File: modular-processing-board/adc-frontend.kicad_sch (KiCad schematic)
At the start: 65 parts, among them J601 Conn_Coaxial_Small, J604 Conn_Coaxial_Small, U1002 THS4521IDGK, U601 LMV321, U602 TL432DBZ, U603 THS4521IDGK

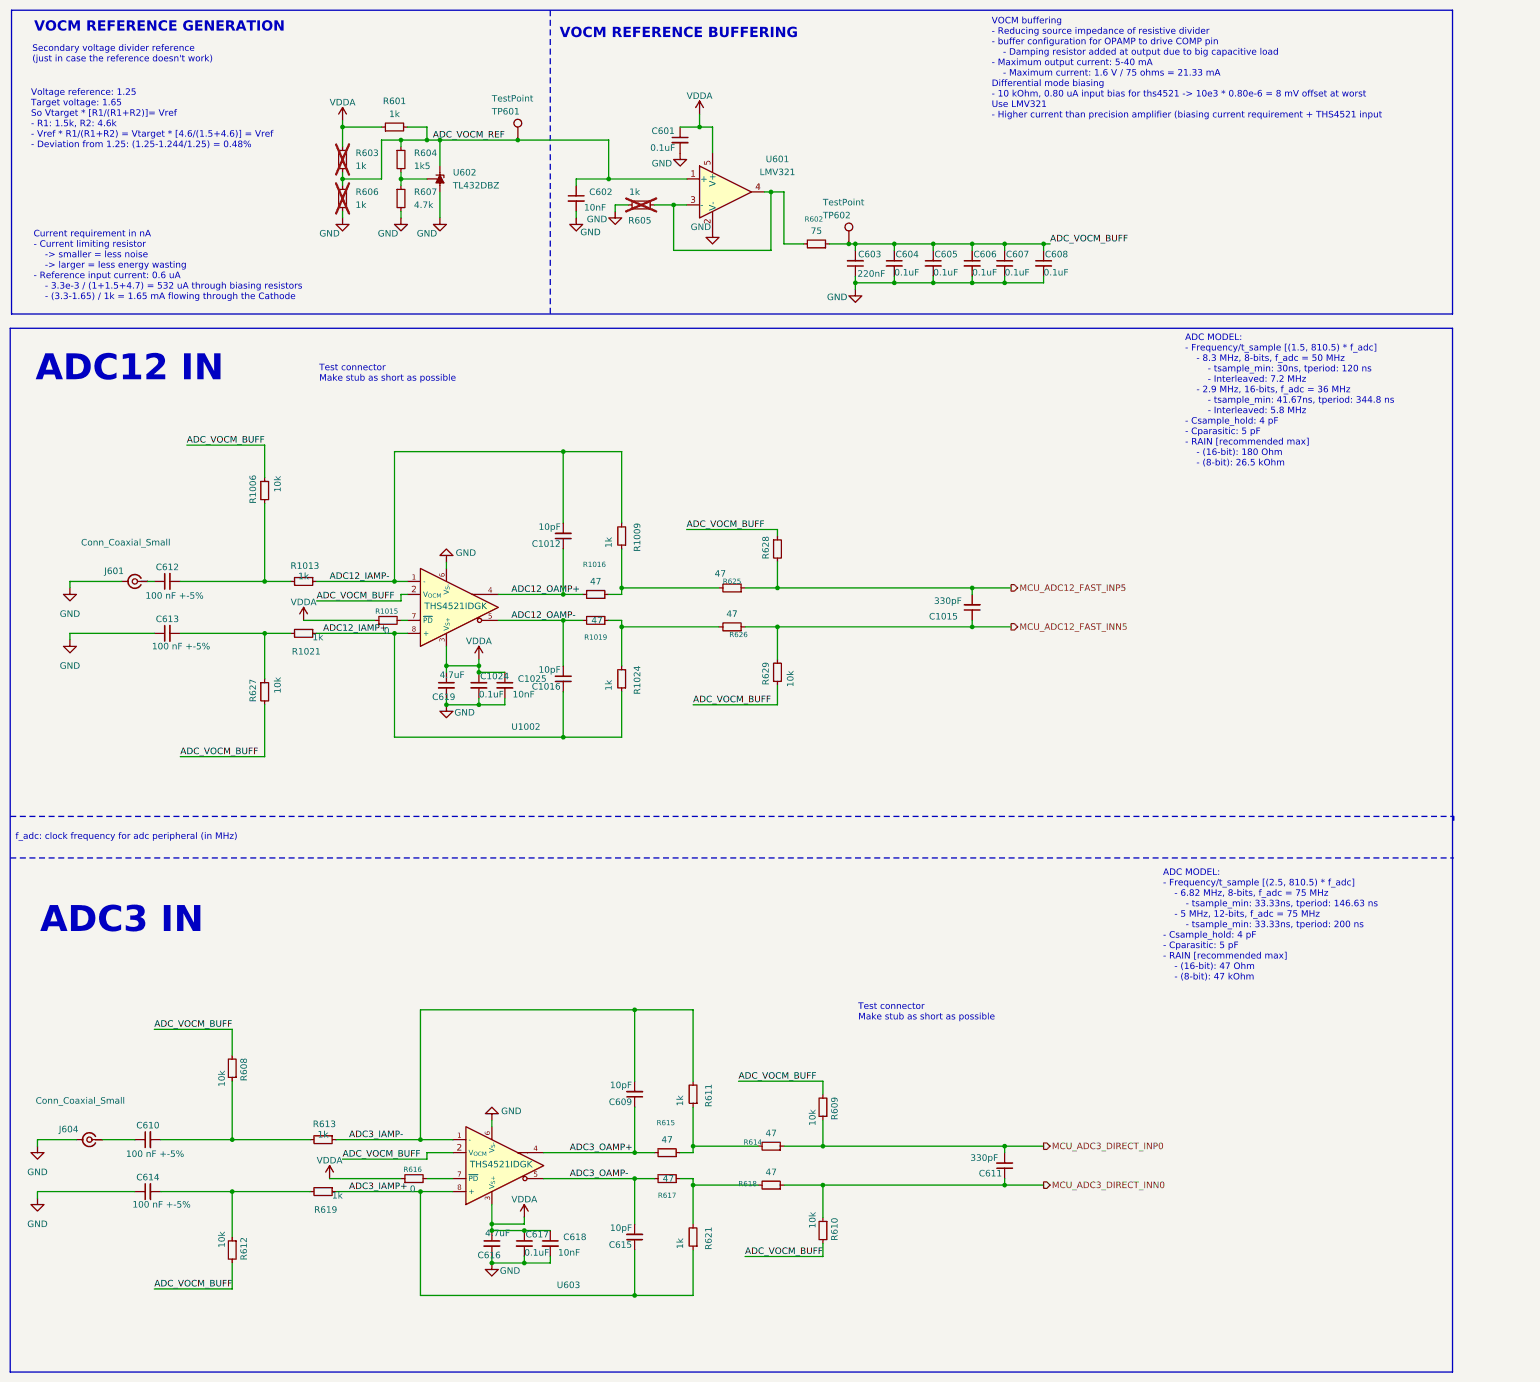
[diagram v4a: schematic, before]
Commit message: replaced sdmmc connector, added smmc trace, added u.fl. connectors
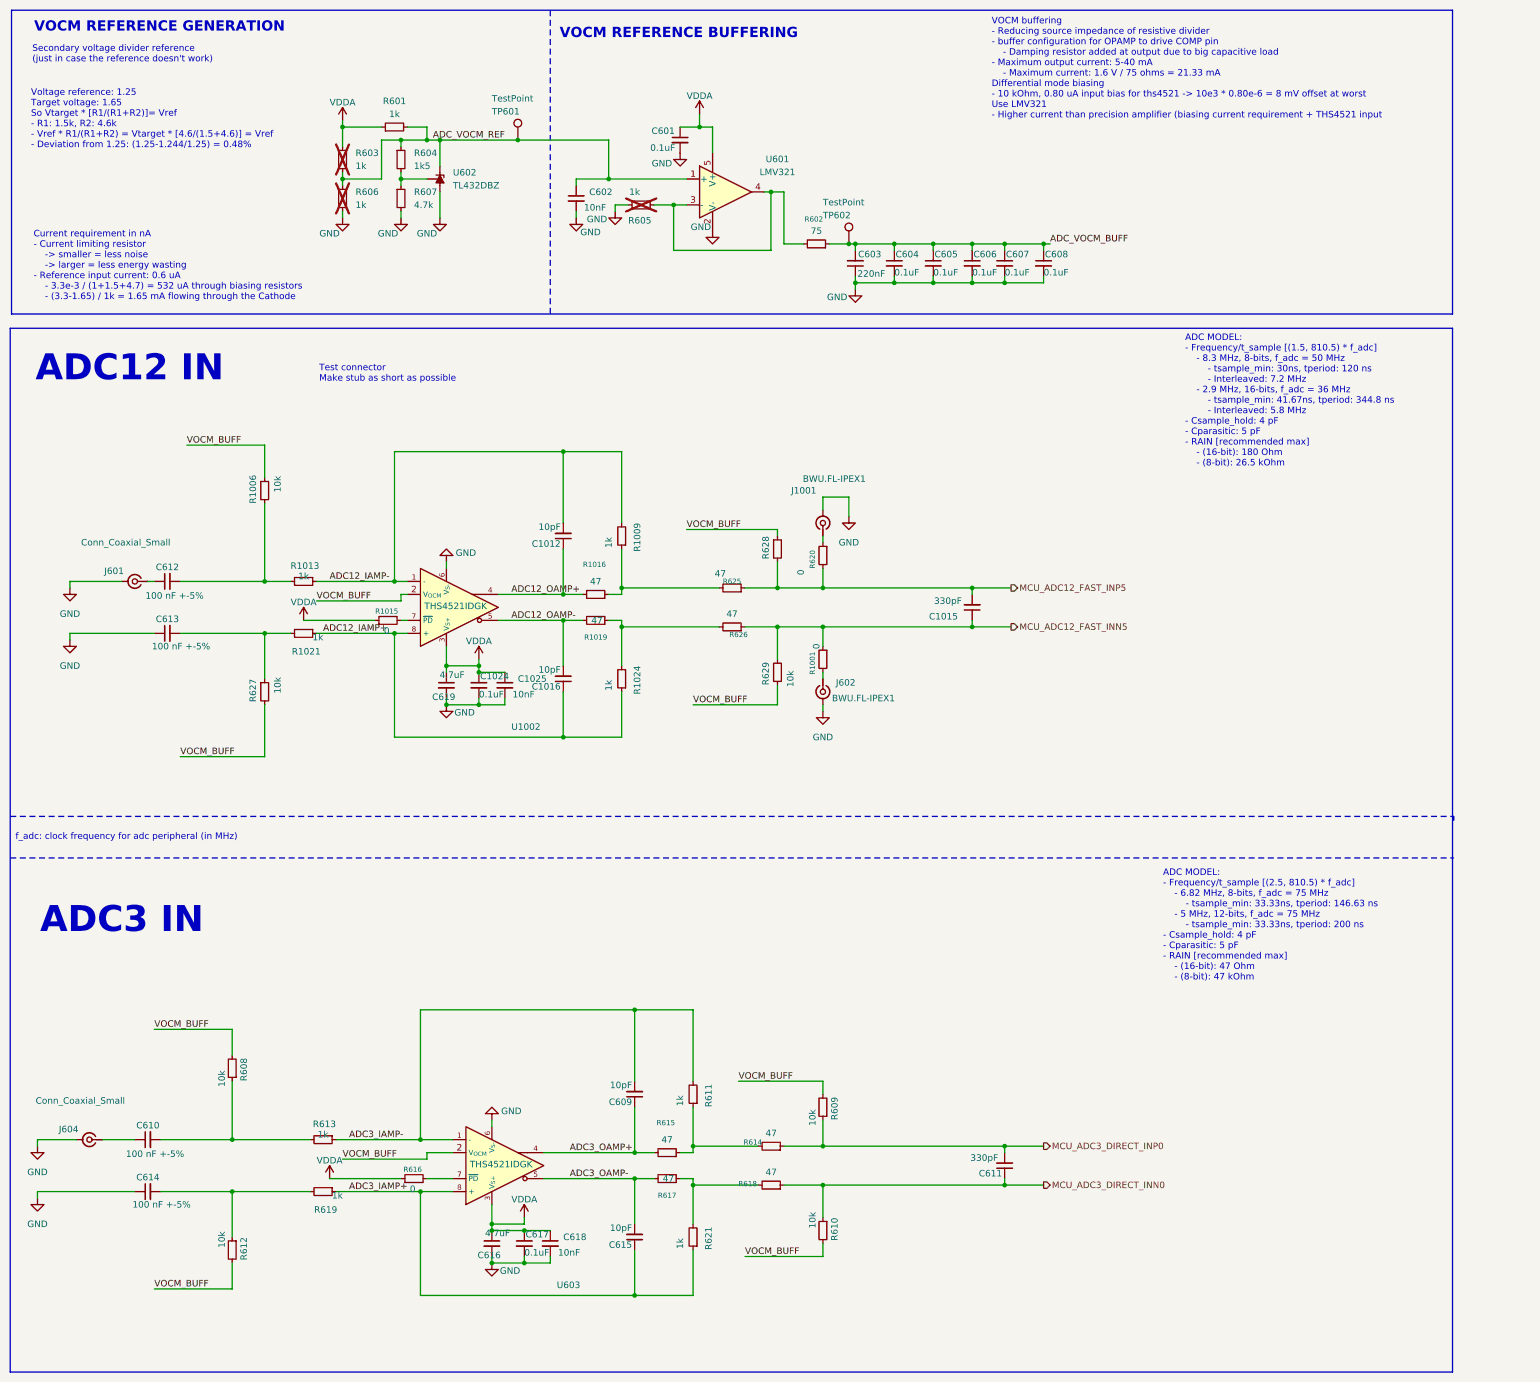
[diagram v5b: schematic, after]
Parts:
- added J1001, J602: BWU.FL-IPEX1, iw-connector:BWU.FL-IPEX1, symbol Connector:Conn_Coaxial_Small
- added R1001, R620: 0, Resistor_SMD:R_0603_1608Metric_Pad0.98x0.95mm_HandSolder, symbol Device:R_Small
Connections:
- net ADC_VOCM_BUFF: no longer R1006.1, R608.2, R609.2, R610.2, R612.2, R627.2, R628.1, R629.1, U1002.2 (V_{OCM}), U603.2 (V_{OCM})
- net GND: now also J1001.2 (Ext), J602.2 (Ext)
- net MCU_ADC12_FAST_INN5: now also R1001.1
- net MCU_ADC12_FAST_INP5: now also R620.2
- new net: J602.1 (In), R1001.2
- new net: J1001.1 (In), R620.1
- new net VOCM_BUFF: R1006.1, R608.2, R609.2, R610.2, R612.2, R627.2, R628.1, R629.1, U1002.2 (V_{OCM}), U603.2 (V_{OCM})

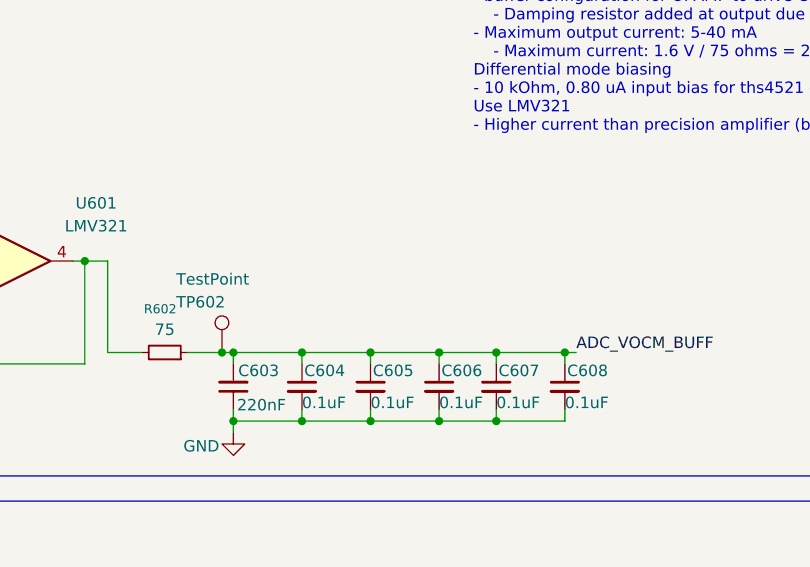
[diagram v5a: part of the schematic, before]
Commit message: reconnected vref
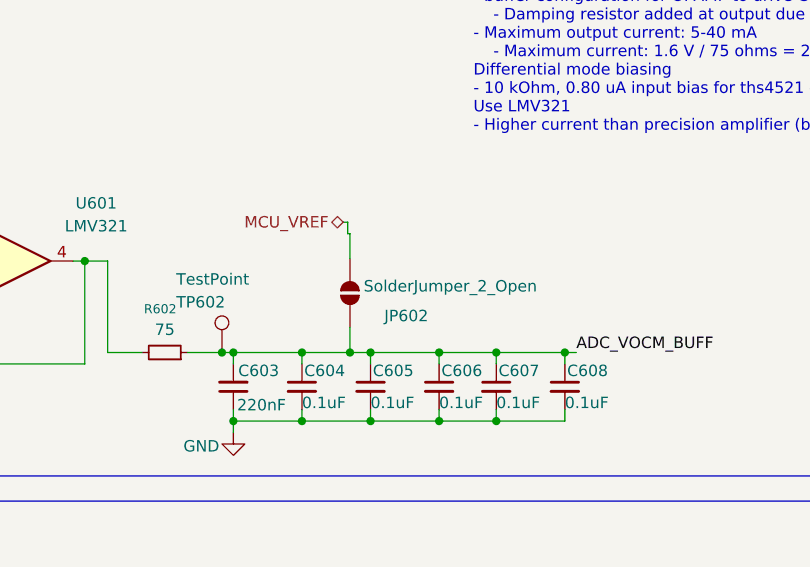
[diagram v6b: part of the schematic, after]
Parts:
- added JP602: SolderJumper_2_Open, Jumper:SolderJumper-2_P1.3mm_Open_Pad1.0x1.5mm, symbol Jumper:SolderJumper_2_Open
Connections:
- net ADC_VOCM_BUFF: now also JP602.1 (A)
- new net MCU_VREF: JP602.2 (B)
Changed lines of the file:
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@@
 	)
 	(junction
+		(at 194.564 59.69)
+		(diameter 0)
+		(color 0 0 0 0)
+	)
+	(junction
 		(at 189.23 67.31)
 		(diameter 0)
@@
 	(wire
 		(pts
+			(xy 189.23 59.69) (xy 194.564 59.69)
+		)
+		(stroke
+			(width 0)
+			(type default)
+		)
+	)
+	(wire
+		(pts
 			(xy 204.47 67.31) (xy 210.82 67.31)
 		)
@@
 	(wire
 		(pts
+			(xy 193.802 45.212) (xy 194.31 45.212)
+		)
+		(stroke
+			(width 0)
+			(type default)
+		)
+	)
+	(wire
+		(pts
 			(xy 100.33 54.61) (xy 100.33 49.53)
 		)
@@
 	(wire
 		(pts
+			(xy 194.31 45.212) (xy 194.31 46.482)
+		)
+		(stroke
+			(width 0)
+			(type default)
+		)
+	)
+	(wire
+		(pts
 			(xy 66.04 110.49) (xy 66.04 125.73)
 		)
@@
 	(wire
 		(pts
+			(xy 194.564 46.482) (xy 194.31 46.482)
+		)
+		(stroke
+			(width 0)
+			(type default)
+		)
+	)
+	(wire
+		(pts
 			(xy 135.89 147.32) (xy 135.89 156.21)
 		)
@@
 	(wire
 		(pts
+			(xy 194.564 56.896) (xy 194.564 59.69)
+		)
+		(stroke
+			(width 0)
+			(type default)
+		)
+	)
+	(wire
+		(pts
 			(xy 92.71 46.99) (xy 97.79 46.99)
 		)
@@
 	(wire
 		(pts
-			(xy 196.85 59.69) (xy 189.23 59.69)
+			(xy 180.34 59.69) (xy 181.61 59.69)
 		)
 		(stroke
@@
 	(wire
 		(pts
-			(xy 180.34 59.69) (xy 181.61 59.69)
+			(xy 160.02 127) (xy 166.37 127)
 		)
 		(stroke
@@
 	(wire
 		(pts
-			(xy 160.02 127) (xy 166.37 127)
+			(xy 138.43 237.49) (xy 142.24 237.49)
 		)
 		(stroke
@@
 	(wire
 		(pts
-			(xy 138.43 237.49) (xy 142.24 237.49)
+			(xy 194.564 59.69) (xy 196.85 59.69)
+		)
+		(stroke
+			(width 0)
+			(type default)
+		)
+	)
+	(wire
+		(pts
+			(xy 194.564 46.482) (xy 194.564 49.276)
 		)
 		(stroke
@@
 		)
 	)
+	(hierarchical_label "MCU_VREF"
+		(shape bidirectional)
+		(at 193.802 45.212 180)
+		(effects
+			(font
+				(size 1.27 1.27)
+			)
+			(justify right)
+		)
+	)
 	(hierarchical_label "MCU_ADC3_DIRECT_INP0"
 		(shape output)
@@
 					(unit 1)
 				)
+			)
+		)
+	)
+	(symbol
+		(lib_id "Jumper:SolderJumper_2_Open")
+		(at 194.564 53.086 90)
+		(unit 1)
+		(exclude_from_sim no)
+		(in_bom no)
+		(on_board yes)
+		(dnp no)
+		(property "Reference" "JP602"
+			(at 198.374 55.6259 90)
+			(effects
+				(font
+					(size 1.27 1.27)
+				)
+				(justify right)
+			)
+		)
+		(property "Value" "SolderJumper_2_Open"
+			(at 196.088 52.3239 90)
+			(effects
+				(font
+					(size 1.27 1.27)
+				)
+				(justify right)
+			)
+		)
+		(property "Footprint" "Jumper:SolderJumper-2_P1.3mm_Open_Pad1.0x1.5mm"
+			(at 194.564 53.086 0)
+			(effects
+				(font
+					(size 1.27 1.27)
+				)
+				(hide yes)
+			)
+		)
+		(property "Datasheet" "~"
+			(at 194.564 53.086 0)
+			(effects
+				(font
+					(size 1.27 1.27)
+				)
+				(hide yes)
+			)
+		)
+		(property "Description" "Solder Jumper, 2-pole, open"
+			(at 194.564 53.086 0)
+			(effects
+				(font
+					(size 1.27 1.27)
+				)
+				(hide yes)
+			)
+		)
+		(pin "2"
+		)
+		(pin "1"
+		)
+		(instances
+			(project "modular-processing-board"
+				(path "/73b5a92f-908b-4f97-a96c-14ee20a7f293/f6ec5a2c-a447-41c5-b01d-0cfa4d0577c8"
+					(reference "JP602")
+					(unit 1)
+				)

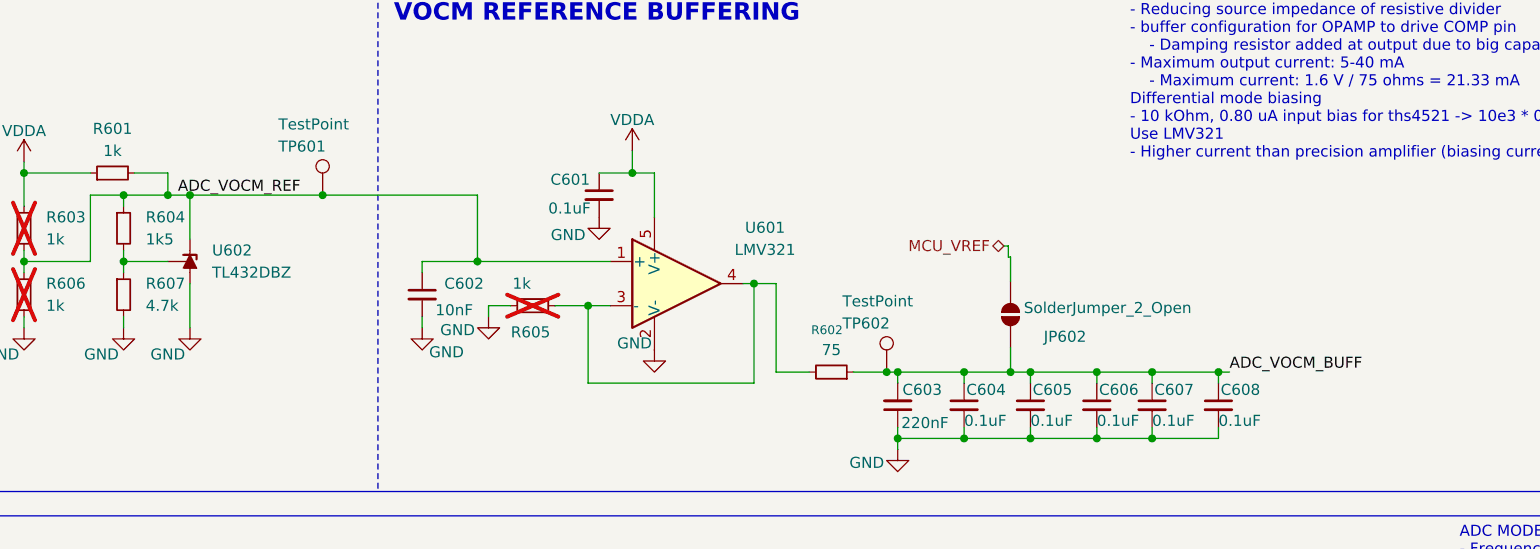
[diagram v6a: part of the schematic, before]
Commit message: layed out most components (next) cadd vias for impedance reduction for high-speed signals, check impedance of signals
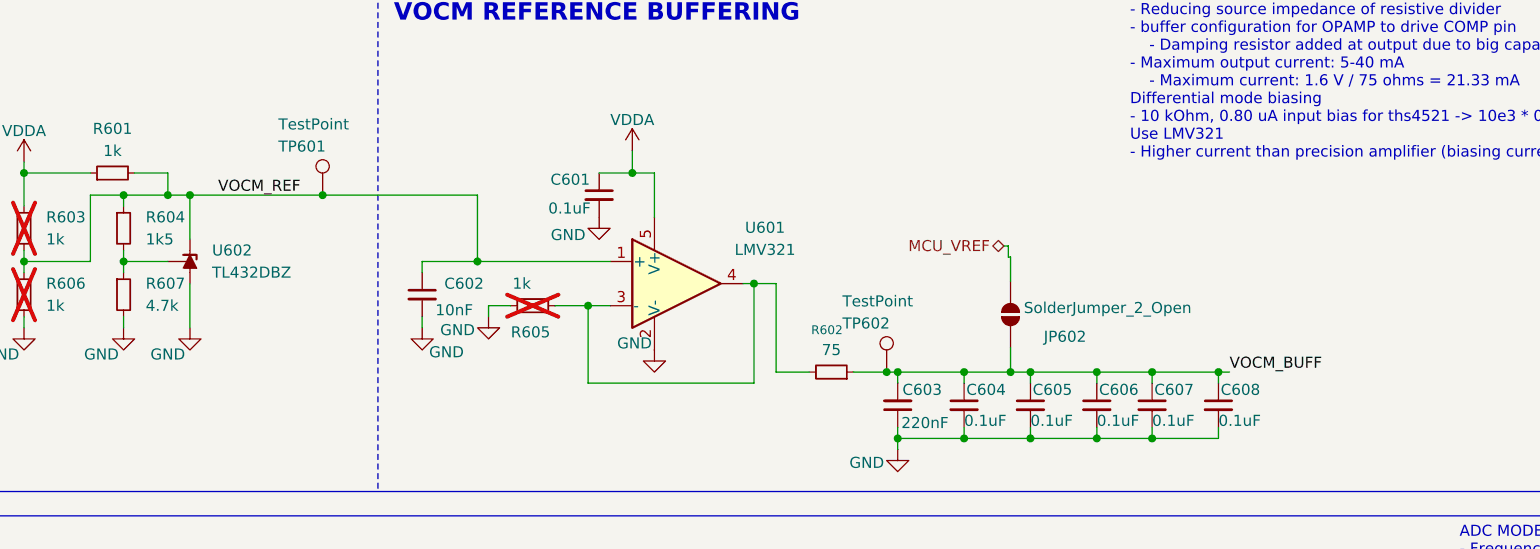
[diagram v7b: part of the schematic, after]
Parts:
- TP601: footprint iw-misc:TestPoint_Pad_D0.5mm -> TestPoint:TestPoint_Pad_1.0x1.0mm
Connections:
- net ADC_VOCM_BUFF is gone; now on net VOCM_BUFF: C603.2, C604.1, C605.1, C606.1, C607.1, C608.1, JP602.1 (A), R602.1, TP602.1
- net ADC_VOCM_REF renamed VOCM_REF
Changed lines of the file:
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@@
 		)
 	)
-	(label "ADC_VOCM_REF"
+	(label "VOCM_REF"
 		(at 113.03 39.37 180)
 		(effects
@@
 		)
 	)
-	(label "ADC_VOCM_BUFF"
+	(label "VOCM_BUFF"
 		(at 219.71 59.69 0)
 		(effects
@@
 			)
 		)
-		(property "Footprint" "iw-misc:TestPoint_Pad_D0.5mm"
+		(property "Footprint" "TestPoint:TestPoint_Pad_1.0x1.0mm"
 			(at 120.65 39.37 0)
 			(effects

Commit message: checked components part numbers (next) board checks
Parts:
- C1012, C1016, C609, C615: LPN (none) -> C1634; MPN (none) -> CL10C100JB8NNNC
- C1015, C611: LPN (none) -> C1664; MPN (none) -> CL10C331JB8NNNC
- C1025, C602, C618: LPN (none) -> C285010; MPN (none) -> 0201B103K250NT
- C603: LPN (none) -> C16772; MPN (none) -> CL05B224KO5NNNC
- C610, C612, C613, C614: LPN (none) -> C88136; MPN (none) -> 0603B104J500NT
- C616, C619: LPN (none) -> C23733; MPN (none) -> CL05A475MP5NRNC
- J1001, J602: LPN (none) -> C5137195; MPN (none) -> BWU.FL-IPEX1
- J601, J604: LPN (none) -> C496549; MPN (none) -> BWSMA-KE-Z001
- R1001, R620: LPN (none) -> C21189; MPN (none) -> 0603WAF0000T5E
- R1006, R608, R609, R610, R612, R627, R628, R629: LPN (none) -> C25804; MPN (none) -> 0603WAF1002T5E
- R1009, R1013, R1021, R1024, R601, R603, R605, R606, R611, R613, R619, R621: LPN (none) -> C21190; MPN (none) -> 0603WAF1001T5E
- R1015, R616: LPN (none) -> C17168; MPN (none) -> 0402WGF0000TCE
- R1016, R1019, R614, R615, R617, R618, R625, R626: LPN (none) -> C23182; MPN (none) -> 0603WAF470JT5E
- R602: LPN (none) -> C4275; MPN (none) -> 0603WAF750JT5E
- R604: LPN (none) -> C22843; MPN (none) -> 0603WAF1501T5E
- R607: LPN (none) -> C23162; MPN (none) -> 0603WAF4701T5E
- U1002, U603: LPN (none) -> C170157; MPN (none) -> THS4521IDGKR
- U601: LPN (none) -> C7972; MPN (none) -> LMV321IDBVR
- U602: LPN (none) -> C5184435; MPN (none) -> TL432
